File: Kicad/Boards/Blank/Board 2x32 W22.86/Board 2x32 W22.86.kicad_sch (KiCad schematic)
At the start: 4 parts, among them IC1 AP7365-33WG-7, J1 Board 2x24 W15.24mm

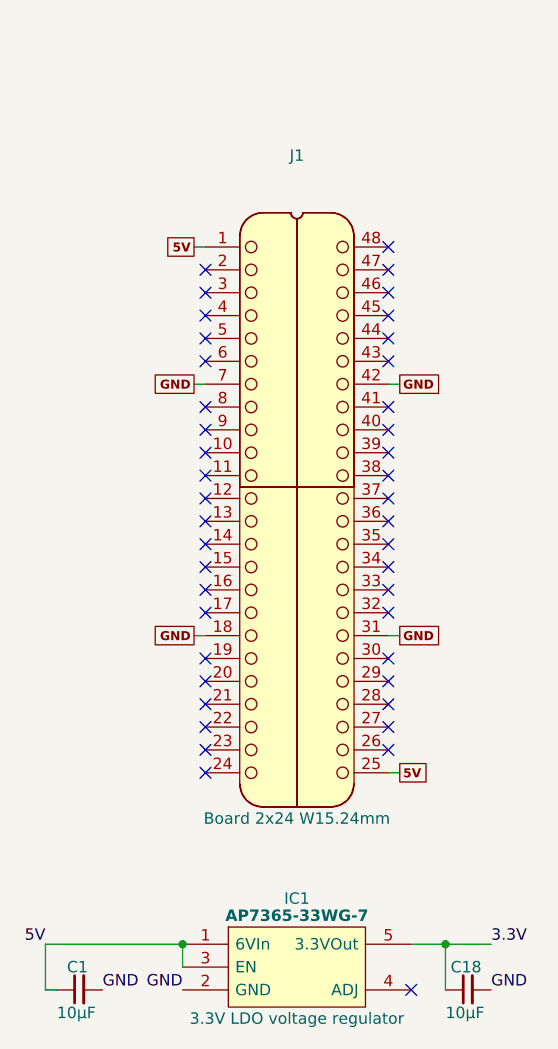
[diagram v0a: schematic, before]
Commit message: Added all blank board projects.
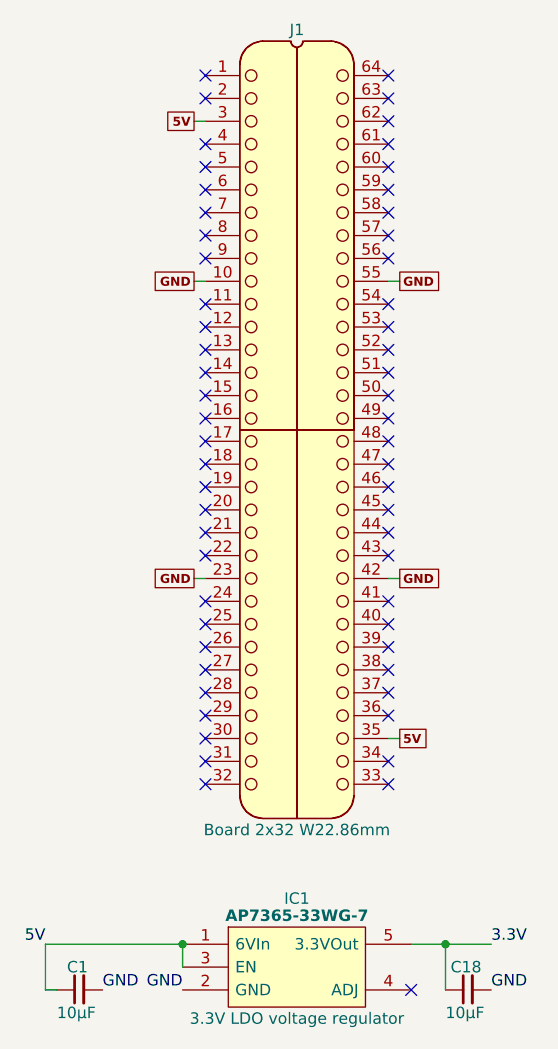
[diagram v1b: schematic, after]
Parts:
- J1: value Board 2x24 W15.24mm -> Board 2x32 W22.86mm; footprint SamacSys_Parts:DIP-48_Board_W15.24mm -> SamacSys_Parts:DIP-64_Board_W22.86mm; symbol HCP65:Board_02x24_W15.24mm -> HCP65:Board_02x32_W22.86mm
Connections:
- net 5V: now also J1.3, J1.35; no longer J1.1, J1.25
- net GND: now also J1.10, J1.23, J1.55; no longer J1.18, J1.31, J1.7
- no-connect marks 43 -> 59
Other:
- title: Board 2x24 W15.24mm -> Board 2x32 W22.86mm
